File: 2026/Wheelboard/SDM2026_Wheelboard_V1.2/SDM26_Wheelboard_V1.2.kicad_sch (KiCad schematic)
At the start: 49 parts, among them IC1 ESP32-S3-WROOM-1-N8R8, IC5 TLP175A_TPL,E, IC6 CP2102N-A02-GQFN28, J2 ESP_USB, J3 Conn_01x04_Socket, J4 JST-XH, J5 Conn_01x02_Socket, J6 Conn_01x02_Socket, Q1 SOT96P237X111-3N, Q2 SOT96P237X111-3N, U3 MIC37100-3.3WS, U4 USBLC6-2SC6, U7 SN65HVD230

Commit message: Fixxed mux and leds and stuff
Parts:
- removed C1: 10uF, Capacitor_SMD:C_0805_2012Metric, symbol Device:C_Small
- removed D1: GREEN, Library:Dialight_561-XX0X-XXX, symbol Device:LED_Small
- removed D3: RED, Library:Dialight_561-XX0X-XXX, symbol Device:LED_Small
- removed J4: JST-XH, Connector_JST:JST_EH_B4B-EH-A_1x04_P2.50mm_Vertical, symbol Connector:Conn_01x04_Pin
- removed R2: 220, Resistor_SMD:R_0805_2012Metric, symbol Device:R_Small
- removed U3: MIC37100-3.3WS, Package_TO_SOT_SMD:SOT-223-3_TabPin2, symbol Library:MIC37100-3.3WS
- added C11, C12, C15: 1uF, Capacitor_SMD:C_0603_1608Metric, symbol Device:C_Small
- added C13, C14: 10uF, Capacitor_SMD:C_0603_1608Metric, symbol Device:C_Small
- added C20, C22: 100nF, Capacitor_SMD:C_0603_1608Metric, symbol Device:C_Small
- added D5: ESDCAN03-2BWY, SDM_MiscFootprint:SOT65P210X110-3N, symbol SDM_ESD:ESDCAN03-2BWY
- added IC4: TPS259250DRCR, SON50P300X300X100-11L-D, symbol SDM_EFUSE:TPS259250DRCR
- added IC7: TPS2116DRLR, SDM_MiscFootprint:SOTFL50P160X60-8L, symbol SDM_LOGIC:TPS2116DRLR
- added IC8: MIC37100-3.3WS, SOT230P700X180-4N, symbol SDM_VOLTAGE_REGULATORS:MIC37100-3.3WS
- added IC9: TLP175A_TPL,E, SDM_MiscFootprint:TLP266J, symbol SDM_OPTOCOUPLERS:TLP175A_TPL,E
- added J4, J7, J8: Conn_01x04_Socket, Connector_JST:JST_XH_S4B-XH-A_1x04_P2.50mm_Horizontal, symbol Connector:Conn_01x04_Socket
- added LED2, LED3: 150060RS75000, SDM_MiscFootprint:LEDC1608X80N, symbol SDM_LED:150060RS75000
- added R12, R16, R17, R27: 10k, Resistor_SMD:R_0603_1608Metric, symbol Device:R_Small
- added R22: 1M, Resistor_SMD:R_0603_1608Metric, symbol Device:R_Small
- added R23: 0, Resistor_SMD:R_0603_1608Metric, symbol Device:R_Small
- added R24: 60.4k, Resistor_SMD:R_0603_1608Metric, symbol Device:R_Small
- added R25: 68, Resistor_SMD:R_0603_1608Metric, symbol Device:R_Small
- added R26: 120, Resistor_SMD:R_0603_1608Metric, symbol Device:R_Small
- added TP1: 5V_ST, TestPoint:TestPoint_Pad_1.5x1.5mm, symbol Connector:TestPoint
- added U8: SN65HVD230, Package_SO:SOIC-8_3.9x4.9mm_P1.27mm, symbol Interface_CAN_LIN:SN65HVD230
- C3: value 10uF -> 100nF; footprint Capacitor_SMD:C_0805_2012Metric -> Capacitor_SMD:C_0402_1005Metric
- C49: value 0.1uF -> 100nF
- C5: value C_Small -> 1uF
- R14: value 300 -> 68
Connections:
- net +3.3V: now also C14.2, C20.1, C22.1, IC8.3 (OUT), J7.2 (Pin_2), J8.2 (Pin_2), LED3.2 (A), U8.3 (VCC)
- net GND: now also C11.1, C12.1, C13.1, C14.1, C15.1, C20.2, C22.2, D5.3, IC4.11 (GND), IC7.1 (GND), IC8.2 (GND_1), IC8.4 (GND_2), IC9.3, J4.1 (Pin_1), J7.1 (Pin_1), J8.1 (Pin_1), LED2.1 (K), R16.1, R24.1, R25.1, R27.1, U8.2 (GND)
- net I2C2_SCL: now also J7.4 (Pin_4), J8.4 (Pin_4)
- net I2C2_SDA: now also J7.3 (Pin_3), J8.3 (Pin_3)
- net VBUS: now also C15.2, IC7.6 (VIN2)
- net VCC: now also C11.2, IC7.3 (VIN1), IC7.5 (MODE), J4.2 (Pin_2), R12.2
- net at R14.2: now also LED2.2 (A)
- net CAN2_RTX: now reaches IC1.13 (IO19)
- net CAN2_RTX: now also U8.1 (D)
- net CAN2_CTX: now reaches IC1.14 (IO20)
- net CAN2_CTX: now also U8.4 (R)
- net CAN1_TERM: now reaches IC1.9 (IO16)
- net CAN1_TERM: now also IC5.1
- net CAN+ renamed CAN1+
- net CAN1+: now also J4.4 (Pin_4); no longer J3.4 (Pin_4)
- net CAN- renamed CAN1-
- net CAN1-: now also J4.3 (Pin_3); no longer J3.3 (Pin_3)
- net CAN_CTX renamed CAN1_CTX
- net CAN1_CTX: now also U7.4 (R); no longer U7.1 (D)
- net CAN_RTX renamed CAN1_RTX
- net CAN1_RTX: now also U7.1 (D); no longer U7.4 (R)
- net CAN_TERM renamed CAN2_TERM
- net CAN2_TERM: now also IC9.1; no longer IC5.1
- new net: IC7.4 (PR1), R12.1, R16.2
- new net: IC4.2 (EN/UVLO), R22.2
- new net: IC7.8 (ST), R17.2, TP1.1
- new net: LED3.1 (K), R25.2
- new net: R27.2, U8.8 (Rs)
- new net: IC9.6, R26.1
- new net +5V: C12.2, C13.2, IC4.6 (OUT_1), IC4.7 (OUT_2), IC4.8 (OUT_3), IC8.1 (IN), R23.2
- new net CAN2+: D5.2, J3.4 (Pin_4), R26.2, U8.7 (CANH)
- new net CAN2-: D5.1, IC9.4, J3.3 (Pin_3), U8.6 (CANL)
- new net EFUSE_IN: IC4.3 (VIN_1), IC4.4 (VIN_2), IC4.5 (VIN_3), IC7.2 (VOUT), IC7.7 (VOUT), R17.1, R22.1, R23.1
- new net ILIM: IC4.10 (ILIM), R24.2
- no-connect marks 46 -> 45
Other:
- note added: "2A Effuse"
- note added: "5v Mux"
- note added: "Power Regulators"
- note added: "Tire Temperature"
- note removed: "VCC = 5V"
- moved on the sheet: C18, C19, C2, C4, C6, C7, D4, IC1, IC5, J3, LED1, R11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
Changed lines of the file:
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@@
 	(generator "eeschema")
 	(generator_version "9.0")
-	(paper "A4")
+	(paper "A3")

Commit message: Added IMU and updated naming conventions
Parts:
- added C1, C8, C9: 100nF, Capacitor_SMD:C_0603_1608Metric, symbol Device:C_Small
- added IC2: ISM330DHCXTR, SDM_MiscFootprint:LSM6DS3USTR, symbol SDM_SENSOR:ISM330DHCXTR
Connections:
- net +3.3V: now also C1.1, C8.1, IC2.5 (VDDIO), IC2.8 (VDD)
- net CAN1_CTX: now also IC1.11 (IO18); no longer IC1.12 (IO8)
- net CAN1_RTX: now also IC1.10 (IO17); no longer IC1.11 (IO18)
- net CAN2_TERM: now also IC1.12 (IO8); no longer IC1.10 (IO17)
- net EFUSE_IN: now also R17.2, C9.2; no longer R17.1
- net GND: now also C1.2, C8.2, C9.1, IC2.6 (GND_1), IC2.7 (GND_2)
- net I2C1_SCL: now also IC2.13 (SCL)
- net I2C1_SDA: now also IC2.14 (SDA)
- net at IC7.8 (ST), TP1.1: now also R17.1; no longer R17.2
- no-connect marks 45 -> 53
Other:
- note added: "IMU"
- moved on the sheet: C7, R17, R4, R6

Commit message: Wheel board update
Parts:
- removed C2, C3: 100nF, Capacitor_SMD:C_0402_1005Metric, symbol Device:C_Small
- removed C4: 100nF, symbol Device:C
- removed C6: 10uF, symbol Device:C
- removed C7: 1uF, symbol Device:C
- removed R1, R3, R4: 10k, symbol Device:R
- removed R14: 68, Resistor_SMD:R_0603_1608Metric, symbol Device:R_Small
- removed R5, R6: 2.2k, symbol Device:R
- removed U2: ~, Package_SO:MAX9924, symbol Amplifier_Audio:MAX9924
- added C1: 10uF, Capacitor_SMD:C_0603_1608Metric, symbol Device:C_Small
- added C14, C15: 100nF, Capacitor_SMD:C_0603_1608Metric, symbol Device:C_Small
- added C22, C7: 1uF, Capacitor_SMD:C_0603_1608Metric, symbol Device:C_Small
- added IC9: MAX9924UAUB+, SOP50P490X110-10L, symbol SDM_SENSOR:MAX9924UAUB+
- added R12, R15: 2.2k, Resistor_SMD:R_0603_1608Metric, symbol Device:R_Small
- added R16, R20, R5: 10k, Resistor_SMD:R_0603_1608Metric, symbol Device:R_Small
- C5: value 1uF -> 100nF; footprint (none) -> Capacitor_SMD:C_0603_1608Metric
- R25: renamed from R19; footprint (none) -> Resistor_SMD:R_0603_1608Metric
- R26: renamed from R18; footprint (none) -> Resistor_SMD:R_0603_1608Metric
- renumbered C14 to C10, C15 to C11, C20 to C12, C22 to C13, C21 to C16, C8 to C17, C45 to C18, C1 to C19, C18 to C2, C48 to C20, C49 to C21, C19 to C3, C11 to C4, C9 to C6, C12 to C8, C13 to C9, D4 to D1, D5 to D2, IC4 to IC1, IC1 to IC2, IC5 to IC3, IC8 to IC4, IC7 to IC5, IC9 to IC6, IC2 to IC7, IC6 to IC8, J7 to J1, J8 to J2, J4 to J3, J3 to J4, J6 to J5, J2 to J6, J5 to J7, LED3 to LED1, LED1 to LED2, LED2 to LED3, R12 to R1, R23 to R10, R26 to R11, R11 to R13, R27 to R14, R9 to R17, R13 to R18, R10 to R19, R16 to R2, R41 to R22, R42 to R23, R15 to R24, R24 to R3, R20 to R4, R22 to R6, R17 to R7, R25 to R8, R21 to R9, U7 to U1, U8 to U2
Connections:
- net +3.3V: now also C5.1, C1.1, C14.2, C15.2, IC9.10 (Vcc), R12.2, R15.1, R5.1
- net CHIP_PU: now also C7.1, R5.2
- net GND: now also C1.2, C14.1, C15.1, C22.1, C7.2, IC9.4 (BIAS), IC9.5 (GND), IC9.6 (ZERO_EN), IC9.9 (INT_THRS)
- net HE_OUTPUT: now also LED3.2 (A), IC9.7 (COUT)
- net I2C1_SCL: now also R12.1
- net I2C1_SDA: now also R15.2
- net at C16.1, R17.2: now also IC9.1 (IN+)
- net at C16.2, R19.2: now also IC9.2 (IN-)
- net at IC8.24 (RTS), Q1.3 (E): now also R20.2
- net at IC8.28 (DTR), Q2.3 (E): now also R16.2
- net at IC8.8 (VBUS), R24.1, R26.1: now also C22.2; no longer C5.1
- net at Q2.2 (B): now also R20.1
- net at Q1.2 (B): now also R16.1
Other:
- moved on the sheet: C10, LED3, R18

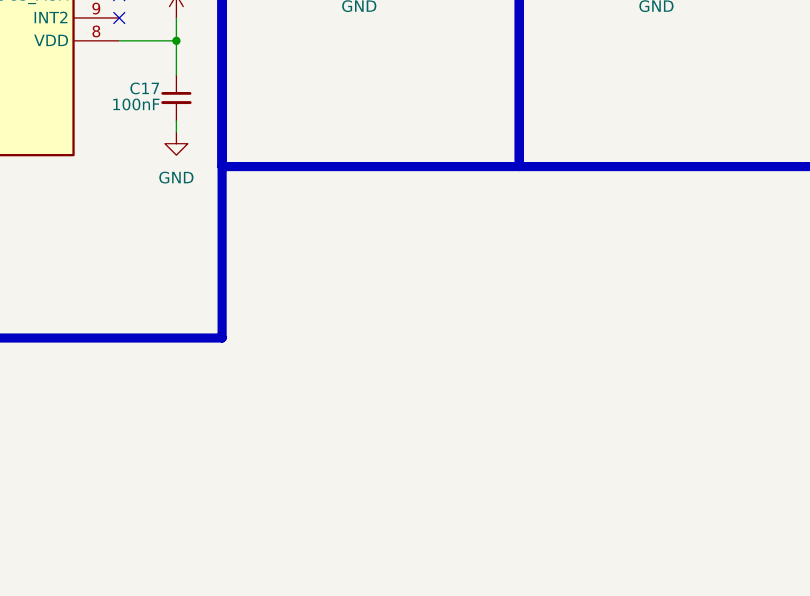
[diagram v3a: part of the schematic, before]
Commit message: wheelboard PCB start
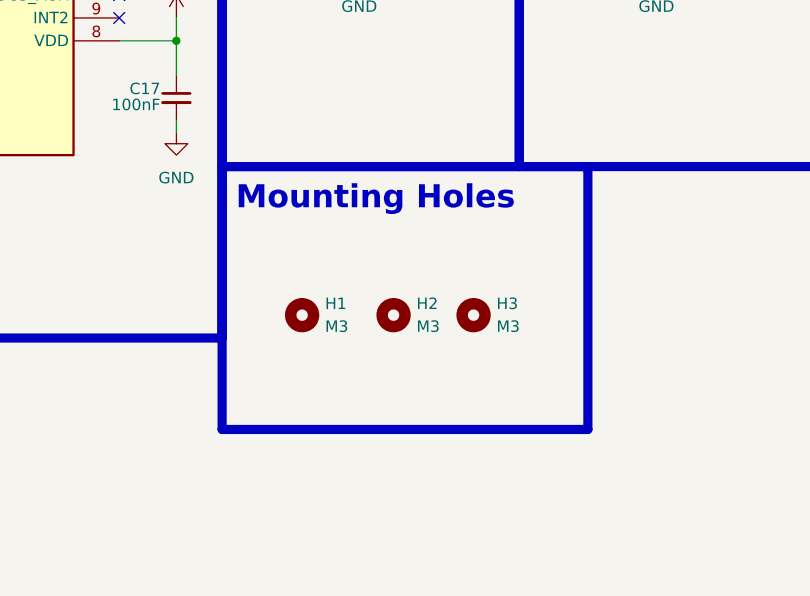
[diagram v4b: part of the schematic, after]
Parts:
- added H1, H2, H3: M3, MountingHole:MountingHole_3.2mm_M3, symbol Mechanical:MountingHole
- J5, J7: footprint Connector_JST:JST_XH_B6B-XH-A_1x02_P2.50mm_Vertical -> Connector_JST:JST_XH_S2B-XH-A_1x02_P2.50mm_Horizontal
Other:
- note added: "Mounting Holes"

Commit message: Wheelboard Progress - added CAN SPI
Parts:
- removed C15: 100nF, Capacitor_SMD:C_0603_1608Metric, symbol Device:C_Small
- added C29, C30: 15pF, Capacitor_SMD:C_0603_1608Metric, symbol Device:C_Small
- added IC10: MCP2518FDT-E_SL, SOIC127P600X175-14L, symbol SDM_CAN:MCP2518FDT-E_SL
- added R55: 1M, Resistor_SMD:R_0603_1608Metric, symbol Device:R_Small
- added Y1: ABM3B-20.000MHZ-10-1-U-T, SDM_MiscFootprint:ABM3B, symbol SDM_CRYSTAL_HSE:ABM3B-20.000MHZ-10-1-U-T
- IC1: footprint SON50P300X300X100-11L-D -> SDM_MiscFootprint:SON50P300X300X100-11L-D
- IC2: footprint ESP32S3WROOM1N8R8 -> SDM_MiscFootprint:ESP32S3WROOM1N8R8
- IC4: footprint SOT230P700X180-4N -> SDM_MiscFootprint:SOT230P700X180-4N
- IC8: footprint QFN50P500X500X80-29N-D -> SDM_MiscFootprint:QFN50P500X500X80-29N-D
- IC9: footprint SOP50P490X110-10L -> SDM_MiscFootprint:SOP50P490X110-10L
- Q1, Q2: footprint Transistors:SOT96P237X111-3N -> SDM_MiscFootprint:SOT96P237X111-3N
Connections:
- net +3.3V: now also J1.4 (Pin_4), J2.4 (Pin_4), IC10.14 (VDD); no longer J1.2 (Pin_2), J2.2 (Pin_2)
- net CAN1+: now also J3.3 (Pin_3); no longer J3.4 (Pin_4)
- net CAN1-: now also J3.2 (Pin_2); no longer J3.3 (Pin_3)
- net CAN2+: now also J4.3 (Pin_3); no longer J4.4 (Pin_4)
- net CAN2-: now also J4.2 (Pin_2); no longer J4.3 (Pin_3)
- net CAN2_CTX: now also U2.1 (D), IC10.1 (TXCAN); no longer IC2.14 (IO20), U2.4 (R)
- net CAN2_RTX: now also U2.4 (R), IC10.2 (RXCAN); no longer IC2.13 (IO19), U2.1 (D)
- net GND: now also C29.1, C30.2, IC10.7 (VSS), Y1.2 (GND_1), Y1.4 (GND_2)
- net I2C2_SCL: now also J1.3 (Pin_3), J2.3 (Pin_3); no longer J1.4 (Pin_4), J2.4 (Pin_4)
- net I2C2_SDA: now also J1.2 (Pin_2), J2.2 (Pin_2); no longer J1.3 (Pin_3), J2.3 (Pin_3)
- net VCC: now also J3.4 (Pin_4), J4.4 (Pin_4); no longer J3.2 (Pin_2), J4.2 (Pin_2)
- net SPI_MOSI: now reaches IC2.17 (IO9)
- net SPI_MOSI: now also IC10.11 (SDI)
- net SPI_SCK: now reaches IC2.18 (IO10)
- net SPI_SCK: now also IC10.10 (SCK)
- net CAN_2_INT: now reaches IC2.19 (IO11)
- net CAN_2_INT: now also IC10.4 (~{INT})
- net CAN_2_INT0: now reaches IC2.20 (IO12)
- net CAN_2_INT0: now also IC10.9 (~{INT0}/GPIO0/XSTBY)
- net CAN_2_INT1: now reaches IC2.21 (IO13)
- net CAN_2_INT1: now also IC10.8 (~{INT1}/GPIO1)
- new net: C29.2, IC10.5 (OSC2), R55.1, Y1.3 (XTAL_2)
- new net: C30.1, IC10.6 (OSC1), R55.2, Y1.1 (XTAL_1)
- new net CAN2_CS: IC10.13 (NCS), IC2.13 (IO19)
- new net SPI_MISO: IC10.12 (SDO), IC2.14 (IO20)
- no-connect marks 53 -> 49
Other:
- note added: "Finding capacitance for HSE Asumming CSTRAY is 3pF,Capacitance load (C_l) given 10pF C_l = C/2 + CSTRAY 10 = C/2 + 3 7 = C/2 C = 14pF using 15 pF"
- moved on the sheet: C12, C13, D2, IC6, R11, R14, U2

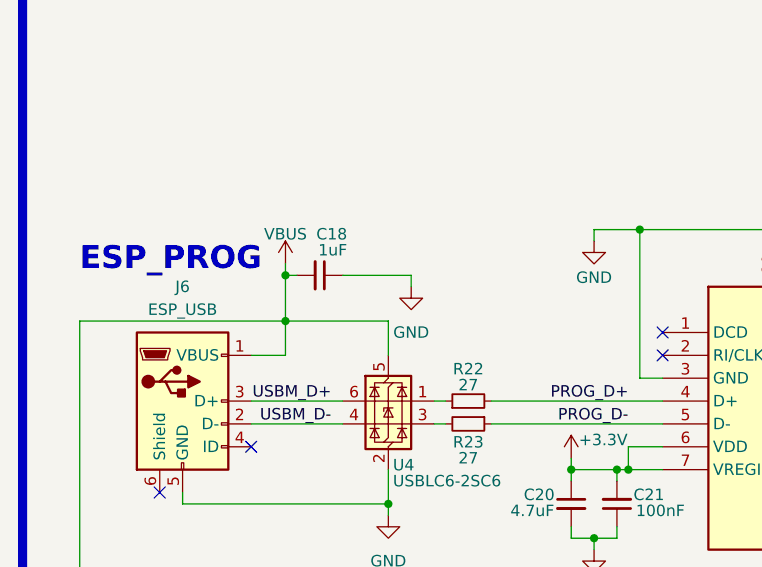
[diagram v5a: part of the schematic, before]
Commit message: Edited pcb layout. Added CAN 2 circuitry
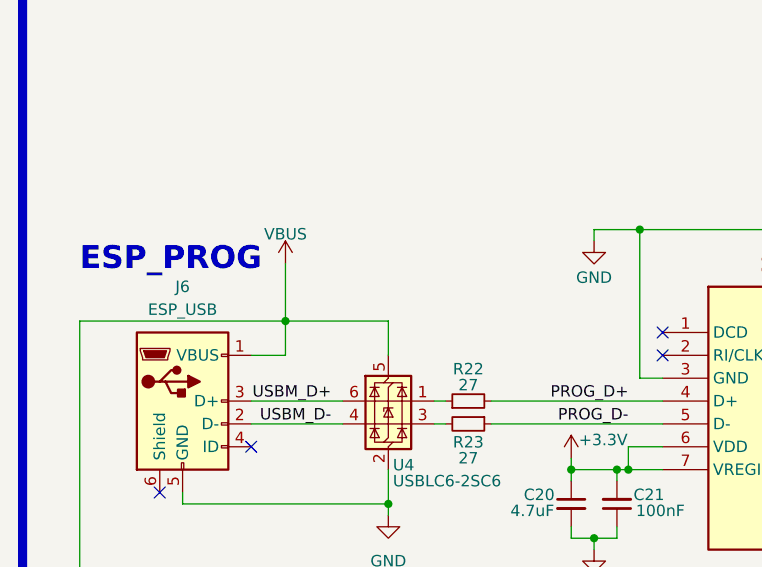
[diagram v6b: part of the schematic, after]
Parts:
- removed C18: 1uF, Capacitor_SMD:C_0603_1608Metric, symbol Device:C_Small
